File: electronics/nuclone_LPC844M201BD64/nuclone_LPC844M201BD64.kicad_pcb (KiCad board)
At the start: 2 copper layers, 48.3 x 76.2 mm, 59 parts, among them J1 JTAG_2X05, J2 USB-ID, J3 nuclone_small_left, J4 nuclone_small_right, SW1 RESET, U1 MCP1702-MB, U2 LPC845M301BD64, Y1 12MHz

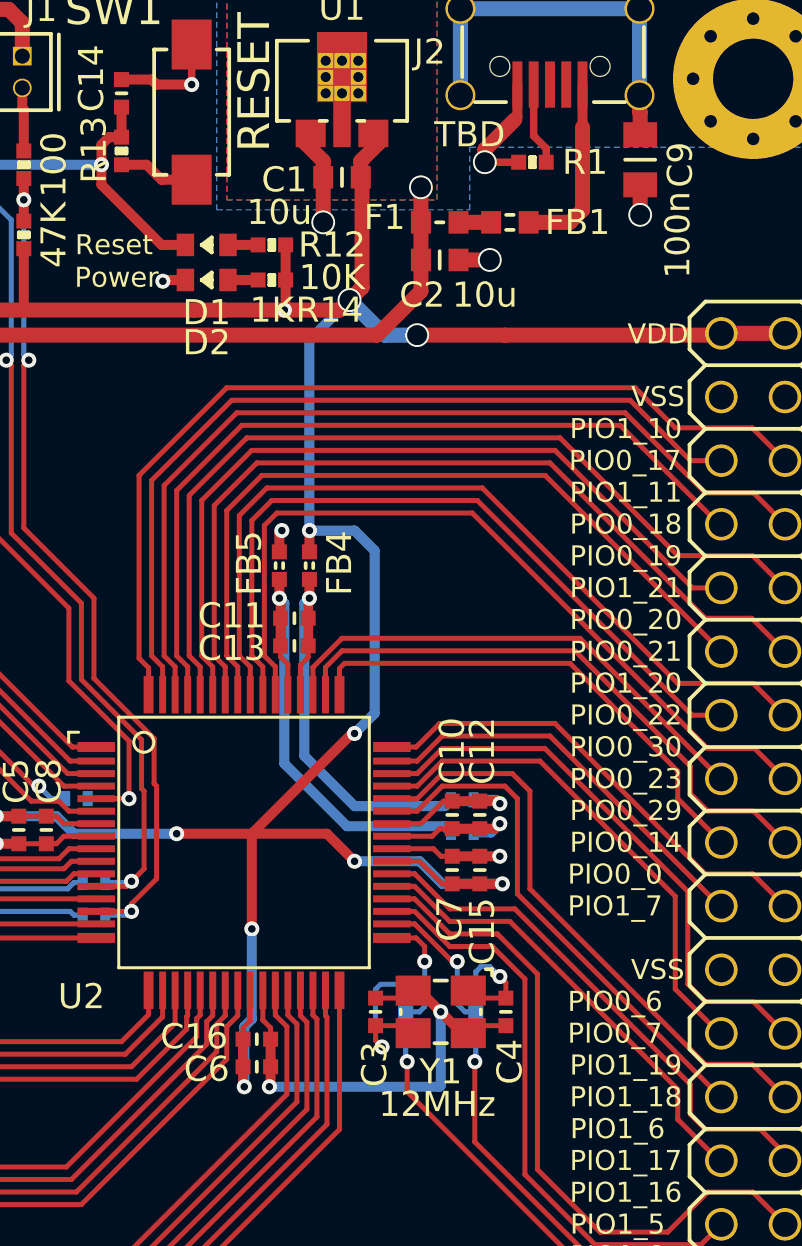
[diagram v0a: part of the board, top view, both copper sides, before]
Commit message: updated versionnumber, changed via sizes, fixed VDD/VSS swap
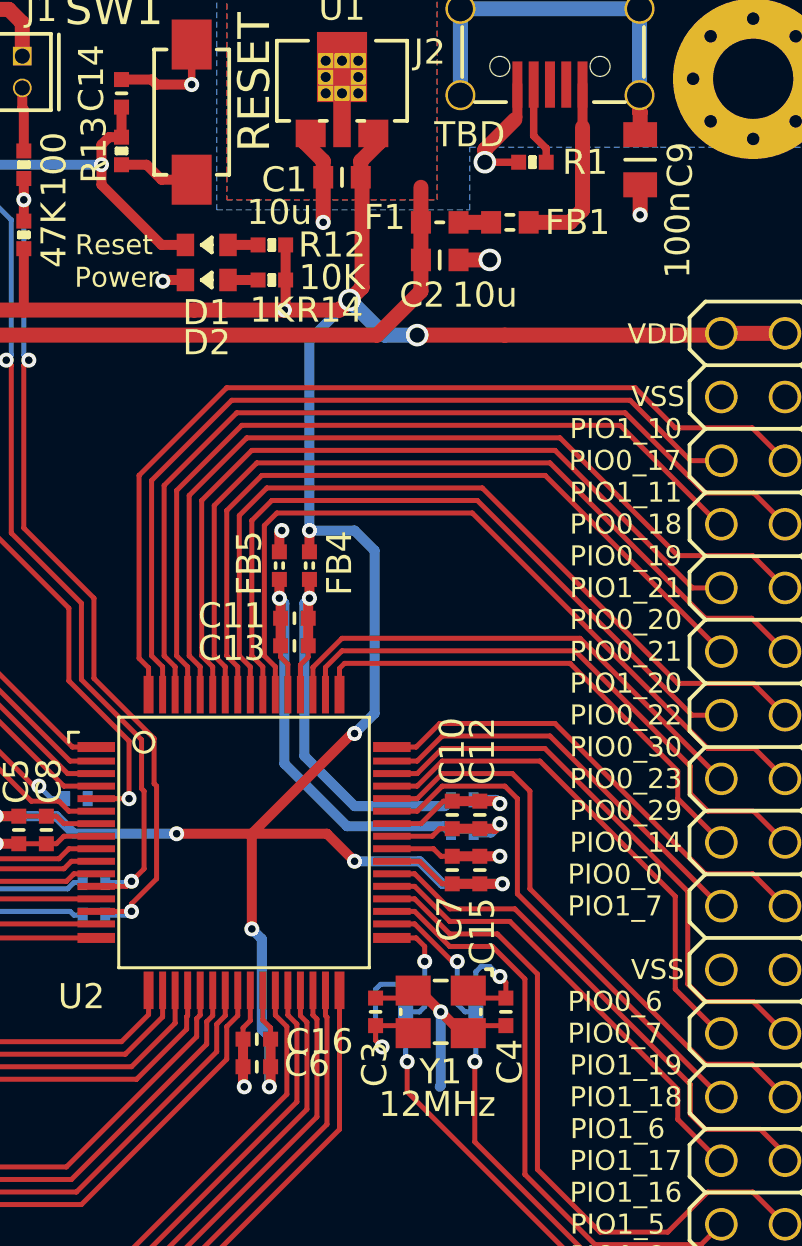
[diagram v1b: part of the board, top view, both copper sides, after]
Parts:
- N2: value 20210406 -> 20210425
- turned C16 to 180 degrees
- turned C6 to 180 degrees
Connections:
- U2 pad 25: /VDD -> /VSS
- U2 pad 26: /VSS -> /VDD
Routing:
- net /VSS: track 46.9 -> 40.1 mm
- net /VBUS: vias 1 -> 0

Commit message: minor copper changes
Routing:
- net /VDD: track 156.0 -> 155.0 mm

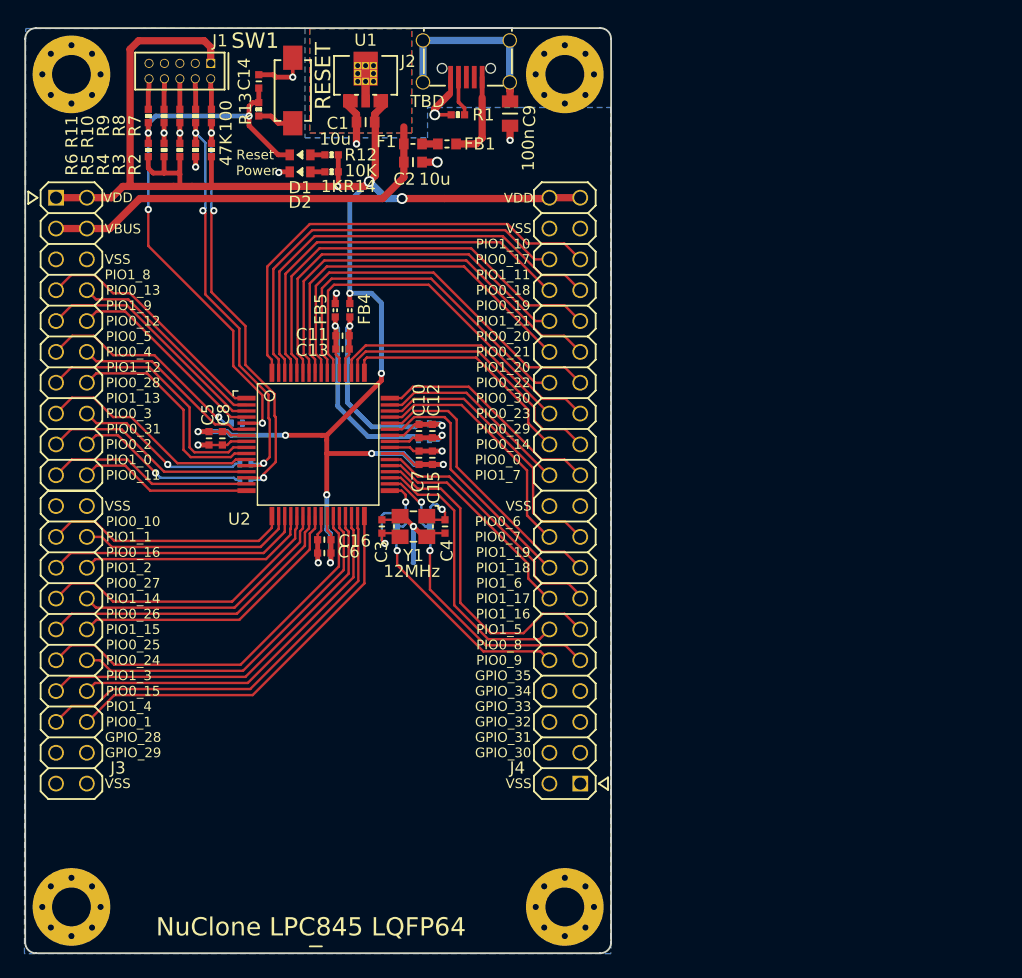
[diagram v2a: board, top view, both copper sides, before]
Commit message: imported components and ripping up old circuits, initial placement
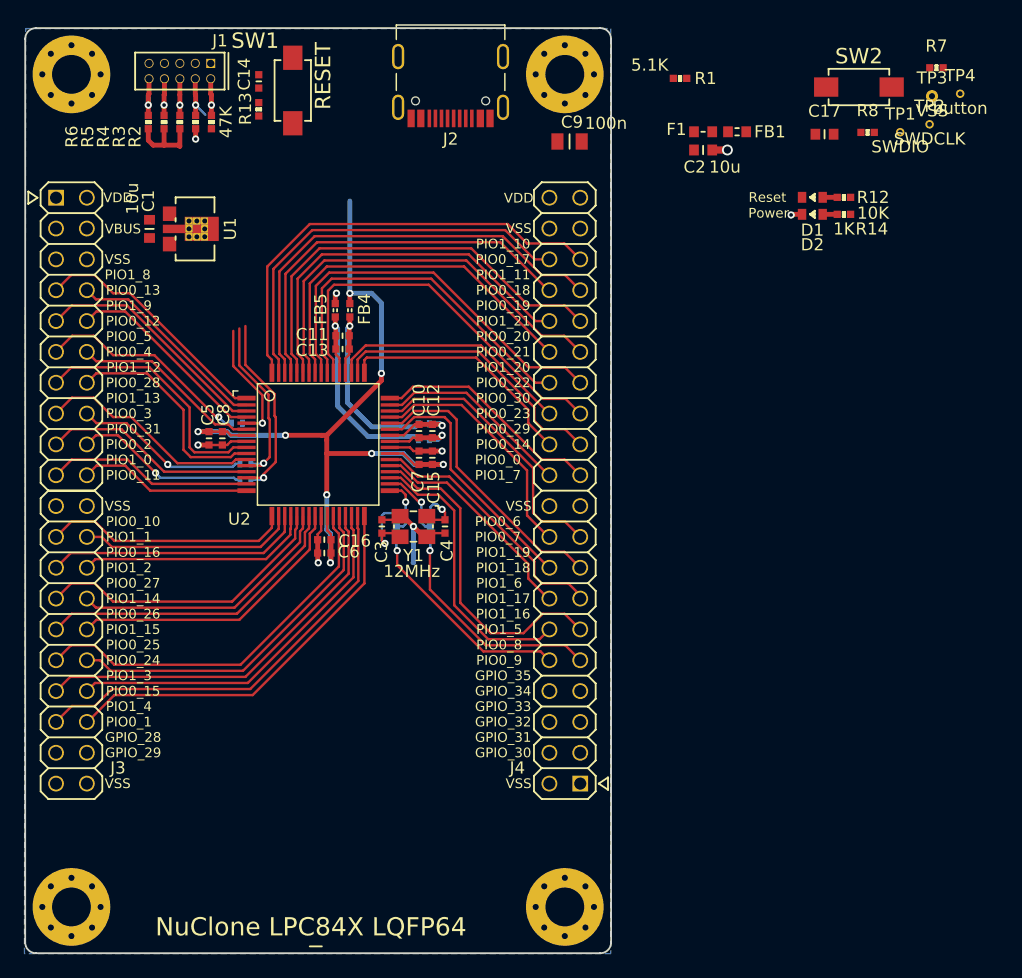
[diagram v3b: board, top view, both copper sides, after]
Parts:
- removed R10, R11, R9: 100, SquantorRcl:R_0402_hand
- added C17: 1u, SquantorRcl:C_0603, F.Cu at (126.8, 69.7)
- added SW2: Bootloader, SquantorSwitches:DTSM3, F.Cu at (129.6, 65.8)
- added TP1: SWDIO, SquantorTestPoints:TestPoint_hole_H04R07, F.Cu at (133.0, 69.5)
- added TP2: SWDCLK, SquantorTestPoints:TestPoint_hole_H04R07, F.Cu at (135.5, 68.9)
- added TP3: VSS, SquantorTestPoints:TestPoint_hole_H05R10, F.Cu at (135.7, 66.6)
- added TP4: button, SquantorTestPoints:TestPoint_hole_H04R07, F.Cu at (138.0, 66.4)
- J2: value USB-ID -> TYPE-C-31-M-12; footprint SquantorUsb:USB-muB-SMD_TH -> SquantorUsb:USB-C-HRO-31-M-12
- N2: value 20210425 -> 20210704
- N4: value NuClone LPC845 LQFP64 -> NuClone LPC84X LQFP64
- R1: value TBD -> 5.1K
- R7: value 100 -> 5.1K
- R8: value 100 -> 10K
- moved R7 59.9 mm to (136.0, 64.2), turned to 0 degrees
- moved R8 55.4 mm to (130.3, 69.5), turned to 0 degrees
- moved D1 42.3 mm to (125.8, 74.9)
- moved D2 42.3 mm to (125.8, 76.3)
- moved R12 42.3 mm to (128.4, 74.9)
- moved R14 42.3 mm to (128.4, 76.3)
- moved C2 23.9 mm to (116.8, 71.0)
- moved F1 23.9 mm to (116.8, 69.5)
- moved FB1 23.9 mm to (119.6, 69.5)
- moved C1 19.9 mm to (71.2, 77.5), turned to 90 degrees
- moved U1 18.9 mm to (74.6, 77.5), turned to 270 degrees
- moved R1 18.5 mm to (114.9, 65.1)
- moved C9 5.41 mm to (105.8, 70.3), turned to 180 degrees
- moved J2 4.88 mm to (96.0, 68.4)
- moved R2 2.30 mm to (76.3, 68.7)
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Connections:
- FB1 pad 2: Net-(FB1-Pad2) -> Net-(C17-Pad2)
- J1 pad 10: Net-(J1-Pad10) -> /RESET
- J1 pad 2: Net-(J1-Pad2) -> /TMS
- J1 pad 4: Net-(J1-Pad4) -> /TCK
- J1 pad 6: Net-(J1-Pad6) -> /TDO
- J1 pad 8: Net-(J1-Pad8) -> /TDI
- R1 pad 2: Net-(J2-Pad4) -> Net-(J2-PadB5)
- R7 pad 1: Net-(J1-Pad2) -> /VSS
- R7 pad 2: /TMS -> Net-(J2-PadA5)
- R8 pad 1: Net-(J1-Pad4) -> /Bootloader
- R8 pad 2: /TCK -> /VDD
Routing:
- net /VDD: track 155.0 -> 75.1 mm, vias 11 -> 8
- net /VBUS: track 34.5 -> 0.00 mm
- net /RESET: track 49.9 -> 15.4 mm, vias 4 -> 2
- net /TMS: track 35.4 -> 19.5 mm, vias 3 -> 2
- net Net-(C9-Pad2): track 15.6 -> 0.00 mm
- net /TCK: track 34.4 -> 19.1 mm, vias 3 -> 2
- net /VSS: track 40.1 -> 25.6 mm, vias 12 -> 8
- net Net-(FB1-Pad2): track 7.36 -> 0.00 mm
- net Net-(J2-Pad4): track 3.31 -> 0.00 mm
- net Net-(R13-Pad2): track 3.05 -> 0.00 mm
- net Net-(J1-Pad10): track 2.54 -> 0.00 mm
- net Net-(J1-Pad2): track 2.54 -> 0.00 mm
- net Net-(J1-Pad8): track 2.53 -> 0.00 mm
- net Net-(J1-Pad4): track 2.53 -> 0.00 mm
- net Net-(J1-Pad6): track 2.52 -> 0.00 mm
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- removed copper zone on B.Cu, net /VBUS
- removed copper zone on F.Cu, net /VBUS

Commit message: place and route done, time for silk placement
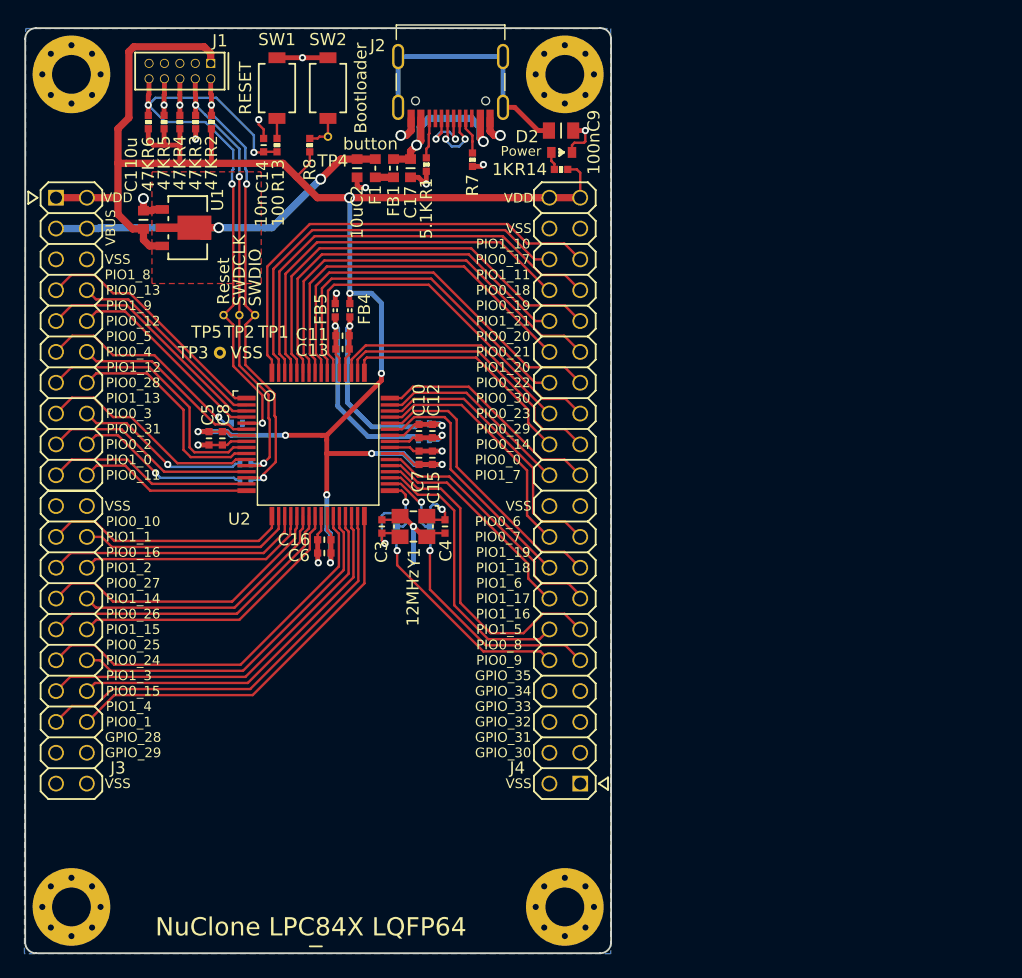
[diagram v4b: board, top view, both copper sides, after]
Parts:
- removed D1: RED, SquantorDiodes:LED_0603_hand
- removed R12: 10K, SquantorRcl:R_0402_hand
- added TP5: Reset, SquantorTestPoints:TestPoint_hole_H04R07, F.Cu at (77.3, 84.6)
- SW1, SW2: footprint SquantorSwitches:DTSM3 -> SquantorSwitches:TD-85XU
- U1: footprint SquantorIC:SOT89-SOT23-Dual-NXP -> SquantorIC:SOT89-NXP
- moved TP3 62.3 mm to (77.0, 87.7)
- moved TP2 59.0 mm to (78.6, 84.6)
- moved TP1 55.2 mm to (79.9, 84.6)
- moved TP4 52.2 mm to (85.9, 69.9)
- moved R8 46.0 mm to (84.4, 70.6), turned to 270 degrees
- moved SW2 43.7 mm to (85.9, 65.9), turned to 270 degrees
- moved R7 39.0 mm to (97.8, 71.8), turned to 90 degrees
- moved C17 34.2 mm to (92.7, 72.5), turned to 90 degrees
- moved C2 28.5 mm to (88.3, 72.5), turned to 90 degrees
- moved FB1 28.5 mm to (91.3, 72.5), turned to 90 degrees
- moved F1 27.2 mm to (89.8, 72.5), turned to 270 degrees
- moved R14 23.6 mm to (105.1, 72.6)
- moved R1 22.1 mm to (94.0, 72.2), turned to 90 degrees
- moved D2 21.3 mm to (105.2, 71.2), turned to 180 degrees
- moved C14 5.27 mm to (80.6, 70.6)
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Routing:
- net /VDD: track 75.1 -> 156.6 mm, vias 8 -> 9
- net /RESET: track 15.4 -> 52.3 mm, vias 2 -> 4
- net /VBUS: track 0.00 -> 32.4 mm, vias 0 -> 2
- net Net-(C9-Pad2): track 0.00 -> 21.6 mm
- net /TMS: track 19.5 -> 39.6 mm, vias 2 -> 3
- net /VSS: track 25.6 -> 44.7 mm, vias 8 -> 15
- net /TCK: track 19.1 -> 37.8 mm, vias 2 -> 3
- net Net-(C17-Pad2): track 0.00 -> 15.5 mm, vias 0 -> 2
- net Net-(J2-PadA6): track 0.00 -> 6.17 mm, vias 0 -> 2
- net Net-(J2-PadA7): track 0.00 -> 5.86 mm, vias 0 -> 2
- net Net-(J2-PadB5): track 0.00 -> 3.42 mm
- net Net-(J2-PadA5): track 0.00 -> 3.08 mm
- net /Bootloader: track 0.00 -> 3.06 mm
- net Net-(R13-Pad2): track 0.00 -> 1.65 mm
- net Net-(F1-Pad2): track 0.00 -> 1.50 mm
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- added copper zone on F.Cu, net /VBUS
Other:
- net class Default: clearance 0.127 -> 0.1; trace_width 0.127 -> 0.2
- net class Power: clearance 0.127 -> 0.1
- net class Signal: clearance 0.127 -> 0.1
- rule trace_clearance: 0.127 -> 0.1
- board text removed: "Reset"

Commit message: switching component values to silk, minor placement updates
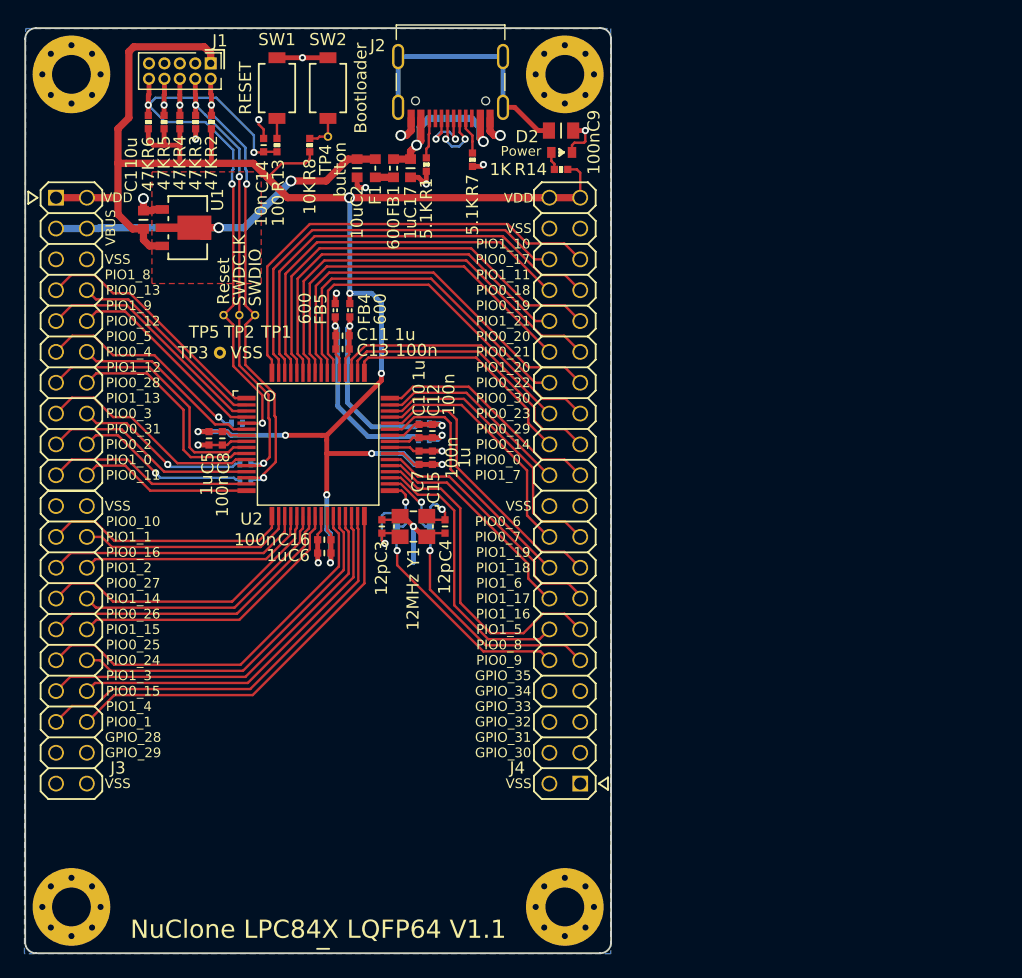
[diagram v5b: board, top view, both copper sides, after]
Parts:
- FB1: value 100 -> 600
- N4: value NuClone LPC84X LQFP64 -> NuClone LPC84X LQFP64 V1.1
- moved N4 0.63 mm to (85.5, 136.2)
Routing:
- net /VDD: track 156.6 -> 158.8 mm

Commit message: updated versionnumber, silk changes, minor routing updates
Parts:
- N2: value 20210704 -> 20210705
- moved TP3 1.08 mm to (76.0, 87.3)
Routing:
- net /RESET: track 52.3 -> 54.2 mm
